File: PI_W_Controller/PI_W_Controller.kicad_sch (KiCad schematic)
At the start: 19 parts, among them J10 Vin Select, J11 Raspberry_Pi_2_3, J12 User Input, J9 OLED, U2 LM7805

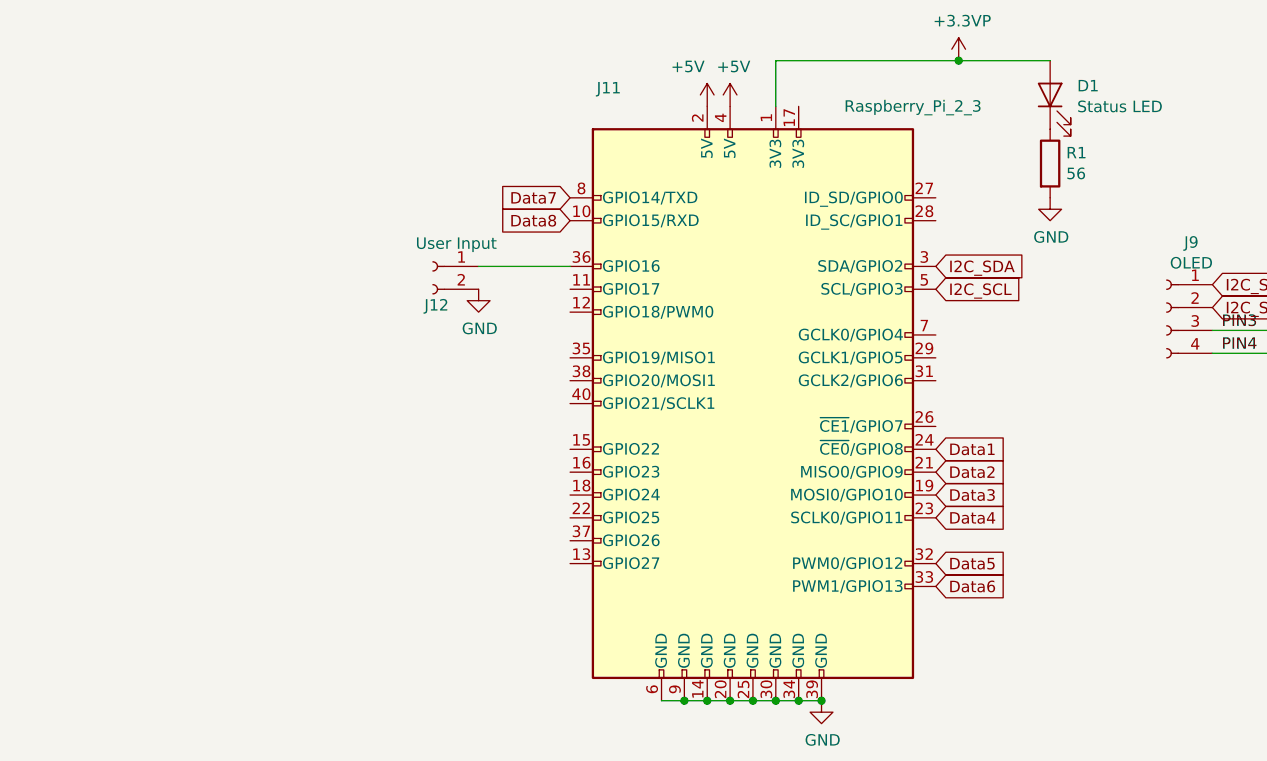
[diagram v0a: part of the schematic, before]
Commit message: changed pinout to match FPP and added Expansion port
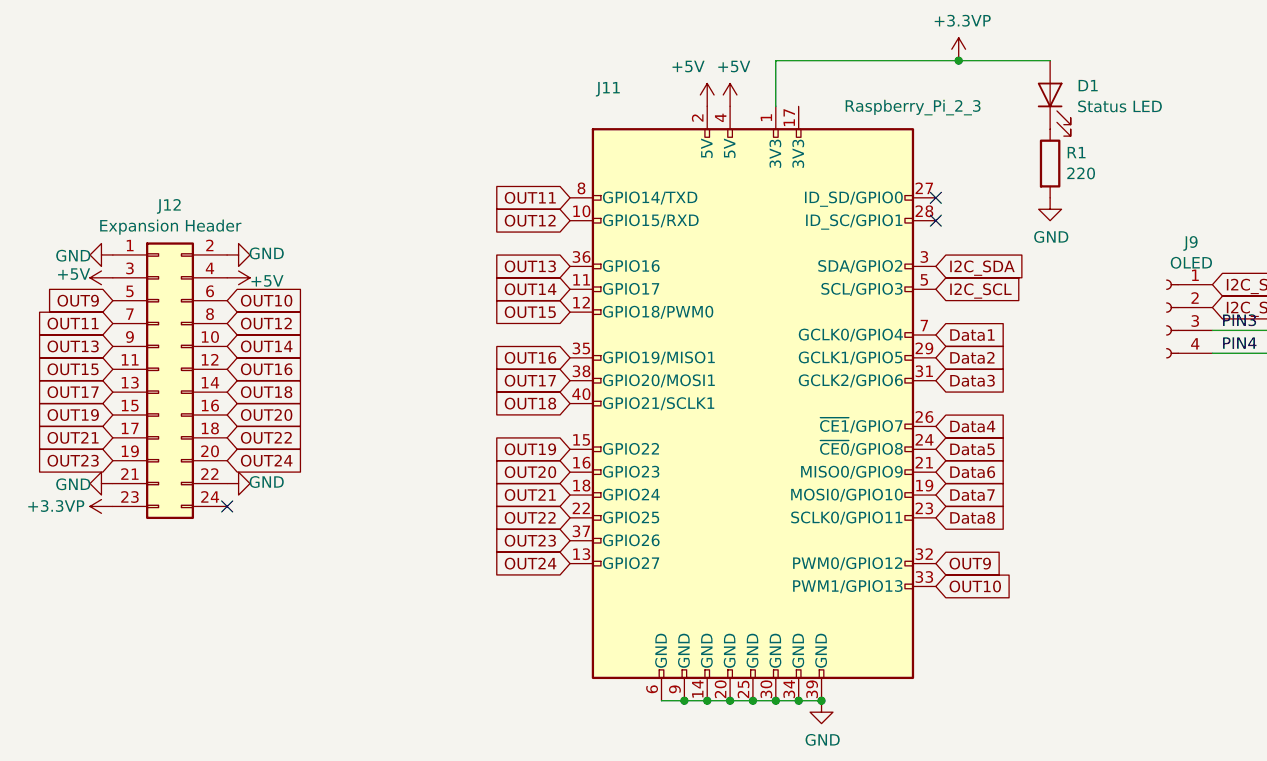
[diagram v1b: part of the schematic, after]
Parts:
- removed J12: User Input, Connector_PinSocket_2.54mm:PinSocket_1x02_P2.54mm_Vertical, symbol Connector:Conn_01x02_Female
- added J12: Expansion Header, 302-S241:OST_302-S241, symbol Connector_Generic:Conn_02x12_Odd_Even
- R1: value 56 -> 220
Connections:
- net +3.3VP: now also J12.23 (Pin_23)
- net +5V: now also J12.3 (Pin_3), J12.4 (Pin_4)
- net Data1: now also J11.7 (GCLK0/GPIO4); no longer J11.24 (~{CE0}/GPIO8)
- net Data2: now also J11.29 (GCLK1/GPIO5); no longer J11.21 (MISO0/GPIO9)
- net Data3: now also J11.31 (GCLK2/GPIO6); no longer J11.19 (MOSI0/GPIO10)
- net Data4: now also J11.26 (~{CE1}/GPIO7); no longer J11.23 (SCLK0/GPIO11)
- net Data5: now also J11.24 (~{CE0}/GPIO8); no longer J11.32 (PWM0/GPIO12)
- net Data6: now also J11.21 (MISO0/GPIO9); no longer J11.33 (PWM1/GPIO13)
- net Data7: now also J11.19 (MOSI0/GPIO10); no longer J11.8 (GPIO14/TXD)
- net Data8: now also J11.23 (SCLK0/GPIO11); no longer J11.10 (GPIO15/RXD)
- net GND: now also J12.1 (Pin_1), J12.2 (Pin_2), J12.21 (Pin_21), J12.22 (Pin_22)
- net OUT13: now reaches J11.36 (GPIO16)
- net OUT13: now also J12.9 (Pin_9)
- net OUT14: now reaches J11.11 (GPIO17)
- net OUT14: now also J12.10 (Pin_10)
- net OUT15: now reaches J11.12 (GPIO18/PWM0)
- net OUT15: now also J12.11 (Pin_11)
- net OUT24: now reaches J11.13 (GPIO27)
- net OUT24: now also J12.20 (Pin_20)
- net OUT19: now reaches J11.15 (GPIO22)
- net OUT19: now also J12.15 (Pin_15)
- net OUT20: now reaches J11.16 (GPIO23)
- net OUT20: now also J12.16 (Pin_16)
- net OUT21: now reaches J11.18 (GPIO24)
- net OUT21: now also J12.17 (Pin_17)
- net OUT22: now reaches J11.22 (GPIO25)
- net OUT22: now also J12.18 (Pin_18)
- net OUT16: now reaches J11.35 (GPIO19/MISO1)
- net OUT16: now also J12.12 (Pin_12)
- net OUT23: now reaches J11.37 (GPIO26)
- net OUT23: now also J12.19 (Pin_19)
- net OUT17: now reaches J11.38 (GPIO20/MOSI1)
- net OUT17: now also J12.13 (Pin_13)
- net OUT18: now reaches J11.40 (GPIO21/SCLK1)
- net OUT18: now also J12.14 (Pin_14)
- new net OUT10: J11.33 (PWM1/GPIO13), J12.6 (Pin_6)
- new net OUT11: J11.8 (GPIO14/TXD), J12.7 (Pin_7)
- new net OUT12: J11.10 (GPIO15/RXD), J12.8 (Pin_8)
- new net OUT9: J11.32 (PWM0/GPIO12), J12.5 (Pin_5)
- no-connect marks 0 -> 3
